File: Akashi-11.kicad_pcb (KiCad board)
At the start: 2 copper layers, 69.9 x 74.9 mm, 2 parts, among them CN10 PPPC192LFBN-RC, CN7 PPPC192LFBN-RC

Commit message: Initial layout of PCB.
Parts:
- added C1: 0.1u, Capacitor_SMD:C_0603_1608Metric_Pad1.08x0.95mm_HandSolder, F.Cu at (170.2, 39.4)
- added C2: 1u, Capacitor_SMD:C_0603_1608Metric_Pad1.08x0.95mm_HandSolder, F.Cu at (143.5, 99.1)
- added C3: 0.1u, Capacitor_SMD:C_0603_1608Metric_Pad1.08x0.95mm_HandSolder, F.Cu at (138.4, 99.1)
- added C4: 1u, Capacitor_SMD:C_0603_1608Metric_Pad1.08x0.95mm_HandSolder, F.Cu at (144.8, 102.0)
- added C5: 0.1u, Capacitor_SMD:C_0603_1608Metric_Pad1.08x0.95mm_HandSolder, F.Cu at (140.1, 69.8)
- added C6: 22u, Capacitor_THT:CP_Radial_D5.0mm_P2.50mm, F.Cu at (166.4, 47.0)
- added C7: 0.1u, Capacitor_SMD:C_0603_1608Metric_Pad1.08x0.95mm_HandSolder, F.Cu at (153.7, 39.4)
- added C8: 0.1u, Capacitor_SMD:C_0603_1608Metric_Pad1.08x0.95mm_HandSolder, F.Cu at (147.3, 69.8)
- added C9: 10u, Capacitor_THT:CP_Radial_D5.0mm_P2.50mm, F.Cu at (153.7, 47.0)
- added D1: D_Schottky, Capacitor_SMD:C_0603_1608Metric_Pad1.08x0.95mm_HandSolder, F.Cu at (142.2, 102.0)
- added D2: D_Schottky, Capacitor_SMD:C_0603_1608Metric_Pad1.08x0.95mm_HandSolder, F.Cu at (143.5, 105.4)
- added D3: LED, LED_THT:LED_D4.0mm, F.Cu at (130.8, 43.2)
- added J1: Conn_02x20_Odd_Even, Connector_PinHeader_2.54mm:PinHeader_2x20_P2.54mm_Vertical, F.Cu at (171.5, 106.7)
- added L1: LQH5BPN4R7N38L, LOCAL_LIB:LQH5BPN100M38L, F.Cu at (175.8, 40.6)
- added L2: LQH5BPN100M38L, LOCAL_LIB:LQH5BPN100M38L, F.Cu at (147.3, 40.6)
- added R1: 1k, Capacitor_SMD:C_0603_1608Metric_Pad1.08x0.95mm_HandSolder, F.Cu at (130.8, 48.3)
- added R2: 61.9, Capacitor_SMD:C_0603_1608Metric_Pad1.08x0.95mm_HandSolder, F.Cu at (151.1, 50.8)
- added R3: 2.15, Capacitor_SMD:C_0603_1608Metric_Pad1.08x0.95mm_HandSolder, F.Cu at (146.1, 50.8)
- added R4: 39, Capacitor_SMD:C_0603_1608Metric_Pad1.08x0.95mm_HandSolder, F.Cu at (176.5, 105.4)
- added R5: 330, Capacitor_SMD:C_0603_1608Metric_Pad1.08x0.95mm_HandSolder, F.Cu at (147.3, 102.0)
- added SW1: SW, Button_Switch_THT:SW_TH_Tactile_Omron_B3F-10xx, F.Cu at (118.7, 40.9)
- added U1: MAX6934AQH+D, Package_LCC:PLCC-44_THT-Socket, F.Cu at (146.1, 77.5)
- added U2: MAX4719EUB+, LOCAL_LIB:MAX4719EUB, F.Cu at (157.5, 104.1)
- added U3: TPS613221ADBV, Package_TO_SOT_SMD:SOT-23-5, F.Cu at (175.3, 48.3)
- added U4: TLV61046ADB, Package_TO_SOT_SMD:SOT-23-6, F.Cu at (147.2, 46.7)
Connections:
- CN10 pad 11: unconnected-(CN10-Pad11) -> /D0
- CN10 pad 12: unconnected-(CN10-Pad12) -> /SPI1_MOSI
- CN10 pad 13: unconnected-(CN10-Pad13) -> /D1
- CN10 pad 15: unconnected-(CN10-Pad15) -> /TIM1_CH1N
- CN10 pad 16: unconnected-(CN10-Pad16) -> /D2
- CN10 pad 17: unconnected-(CN10-Pad17) -> /D3
- CN10 pad 19: unconnected-(CN10-Pad19) -> /D4
- CN10 pad 20: unconnected-(CN10-Pad20) -> GND
- CN10 pad 21: unconnected-(CN10-Pad21) -> /TIM2_CH1
- CN10 pad 22: unconnected-(CN10-Pad22) -> /D5
- CN10 pad 23: unconnected-(CN10-Pad23) -> /TIM1_CH1
- CN10 pad 24: unconnected-(CN10-Pad24) -> /D6
- CN10 pad 25: unconnected-(CN10-Pad25) -> /D7
- CN10 pad 27: unconnected-(CN10-Pad27) -> /D8
- CN10 pad 29: unconnected-(CN10-Pad29) -> /KEY3
- CN10 pad 31: unconnected-(CN10-Pad31) -> /KEY2
- CN10 pad 32: unconnected-(CN10-Pad32) -> GND
- CN10 pad 33: unconnected-(CN10-Pad33) -> /KEY1
- CN10 pad 36: unconnected-(CN10-Pad36) -> /SPI1_SCK
- CN10 pad 9: unconnected-(CN10-Pad9) -> GND
- CN7 pad 1: unconnected-(CN7-Pad1) -> /LOAD
- CN7 pad 12: unconnected-(CN7-Pad12) -> +3V3
- CN7 pad 14: unconnected-(CN7-Pad14) -> Net-(CN7-Pad14)
- CN7 pad 16: unconnected-(CN7-Pad16) -> +3V3
- CN7 pad 19: unconnected-(CN7-Pad19) -> GND
- CN7 pad 2: unconnected-(CN7-Pad2) -> Net-(CN7-Pad2)
- CN7 pad 20: unconnected-(CN7-Pad20) -> GND
- CN7 pad 22: unconnected-(CN7-Pad22) -> GND
- CN7 pad 3: unconnected-(CN7-Pad3) -> /BLANK
- CN7 pad 8: unconnected-(CN7-Pad8) -> GND
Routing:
- net unconnected-(CN7-Pad1): track 2.69 -> 0.00 mm
- net /LOAD: track 0.00 -> 2.69 mm
- net unconnected-(CN7-Pad3): track 2.69 -> 0.00 mm
- net /BLANK: track 0.00 -> 2.69 mm
- added copper zone on B.Cu, net GND
- added copper zone on F.Cu, net GND
- removed copper zone on B.Cu, net unconnected-(CN10-Pad9)
- removed copper zone on F.Cu, net unconnected-(CN10-Pad9)

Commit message: Routing finished
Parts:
- added JP1: Jumper_2_Bridged, Jumper:SolderJumper-2_P1.3mm_Bridged_RoundedPad1.0x1.5mm, F.Cu at (175.9, 51.4)
- added JP2: Jumper_2_Bridged, Jumper:SolderJumper-2_P1.3mm_Bridged_RoundedPad1.0x1.5mm, F.Cu at (151.8, 61.0)
- added TP1: TestPoint, TestPoint:TestPoint_Loop_D1.80mm_Drill1.0mm_Beaded, F.Cu at (142.2, 106.7)
- added TP10: TestPoint, TestPoint:TestPoint_Loop_D1.80mm_Drill1.0mm_Beaded, F.Cu at (158.8, 99.1)
- added TP11: TestPoint, TestPoint:TestPoint_Loop_D1.80mm_Drill1.0mm_Beaded, F.Cu at (163.8, 105.4)
- added TP12: TestPoint, TestPoint:TestPoint_Loop_D1.80mm_Drill1.0mm_Beaded, F.Cu at (157.5, 106.7)
- added TP13: TestPoint, TestPoint:TestPoint_Loop_D1.80mm_Drill1.0mm_Beaded, F.Cu at (146.1, 100.3)
- added TP2: TestPoint, TestPoint:TestPoint_Loop_D1.80mm_Drill1.0mm_Beaded, F.Cu at (130.8, 105.4)
- added TP3: TestPoint, TestPoint:TestPoint_Loop_D1.80mm_Drill1.0mm_Beaded, F.Cu at (181.6, 48.3)
- added TP4: TestPoint, TestPoint:TestPoint_Loop_D1.80mm_Drill1.0mm_Beaded, F.Cu at (181.6, 43.2)
- added TP5: TestPoint, TestPoint:TestPoint_Loop_D1.80mm_Drill1.0mm_Beaded, F.Cu at (176.5, 104.1)
- added TP6: TestPoint, TestPoint:TestPoint_Loop_D1.80mm_Drill1.0mm_Beaded, F.Cu at (176.5, 72.4)
- added TP7: TestPoint, TestPoint:TestPoint_Loop_D1.80mm_Drill1.0mm_Beaded, F.Cu at (151.8, 55.9)
- added TP8: TestPoint, TestPoint:TestPoint_Loop_D1.80mm_Drill1.0mm_Beaded, F.Cu at (127.0, 69.8)
- added TP9: TestPoint, TestPoint:TestPoint_Loop_D1.80mm_Drill1.0mm_Beaded, F.Cu at (127.0, 63.5)
- moved C6 16.5 mm to (181.6, 53.4), turned to -90 degrees
- moved R4 16.3 mm to (160.4, 102.6), turned to 180 degrees
- moved D1 6.35 mm to (135.9, 102.0)
- moved C2 6.35 mm to (137.2, 99.1)
- moved C3 6.35 mm to (132.1, 99.1)
- moved C4 6.35 mm to (138.4, 102.0)
- moved D2 6.35 mm to (137.2, 105.4)
- moved R5 6.35 mm to (141.0, 102.0)
- moved U2 5.24 mm to (152.4, 102.9)
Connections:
- C6 pad 1: +3V3 -> Net-(C6-Pad1)
- C9 pad 1: +24V -> Net-(C9-Pad1)
- CN10 pad 11: /D0 -> /KD0
- CN10 pad 13: /D1 -> /KD1
- CN10 pad 16: /D2 -> /KD2
- CN10 pad 17: /D3 -> /KD3
- CN10 pad 19: /D4 -> /KD4
- CN10 pad 22: /D5 -> /KD5
- CN10 pad 24: /D6 -> /KD6
- CN10 pad 25: /D7 -> /KD7
- CN10 pad 27: /D8 -> /KD8
- J1 pad 12: /D8 -> /KD8
- J1 pad 14: /D7 -> /KD7
- J1 pad 16: /D6 -> /KD6
- J1 pad 18: /D5 -> /KD5
- J1 pad 20: /D4 -> /KD4
- J1 pad 22: /D3 -> /KD3
- J1 pad 24: /D2 -> /KD2
- J1 pad 26: /D1 -> /KD1
- J1 pad 28: /D0 -> /KD0
- R2 pad 1: +24V -> Net-(C9-Pad1)
- U3 pad 4: +3V3 -> Net-(C6-Pad1)
- U4 pad 5: +24V -> Net-(C9-Pad1)
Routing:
- net /TIM2_CH1: track 0.00 -> 62.1 mm
- net +BATT: track 0.00 -> 56.4 mm
- net /SPI1_SCK: track 0.00 -> 52.2 mm
- net /TIM1_CH1: track 0.00 -> 47.8 mm
- net /LOAD: track 2.69 -> 46.9 mm
- net /Seg_a: track 0.00 -> 41.4 mm
- net /TIM1_CH1N: track 0.00 -> 40.6 mm
- net /SPI1_MOSI: track 0.00 -> 39.2 mm
- net Net-(CN7-Pad14): track 0.00 -> 38.8 mm
- net /BLANK: track 2.69 -> 40.9 mm
- net /D8: track 0.00 -> 32.1 mm
- net /D0: track 0.00 -> 27.8 mm
- net /D7: track 0.00 -> 26.4 mm
- net /Seg_g: track 0.00 -> 25.5 mm
- net +24V: track 0.00 -> 25.4 mm
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- added copper zone on B.Cu, net +3V3
- removed copper zone on B.Cu, net GND
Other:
- board text added: "+24V"
- board text added: "+3.3V"
- board text added: "-2.5V"
- board text added: "Akashi-11 v1.0.0 https://github.com/suikan4github/Akashi-11 (C) Seiichi Horie 2022"
- board text added: "BLANK"
- board text added: "GND"
- board text added: "H1"
- board text added: "H2"
- board text added: "LOAD"
- board text added: "RESET"
- board text added: "SPI1_MOSI"
- board text added: "SPI1_SCK"
- board text added: "TIM1_CH1"
- board text added: "TIM1_CH1N"
- board text added: "TIM2_CH1"

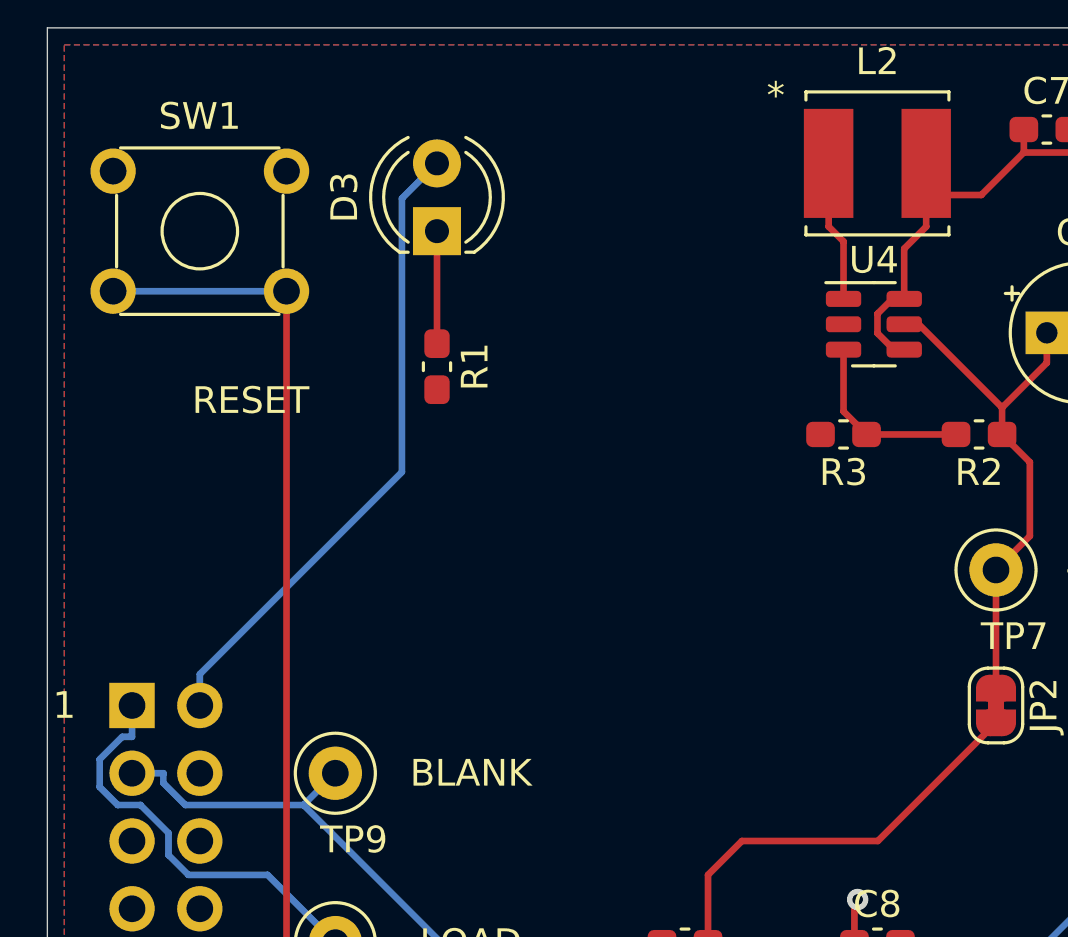
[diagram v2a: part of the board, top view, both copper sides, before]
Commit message: Add EN24 signal and description of README
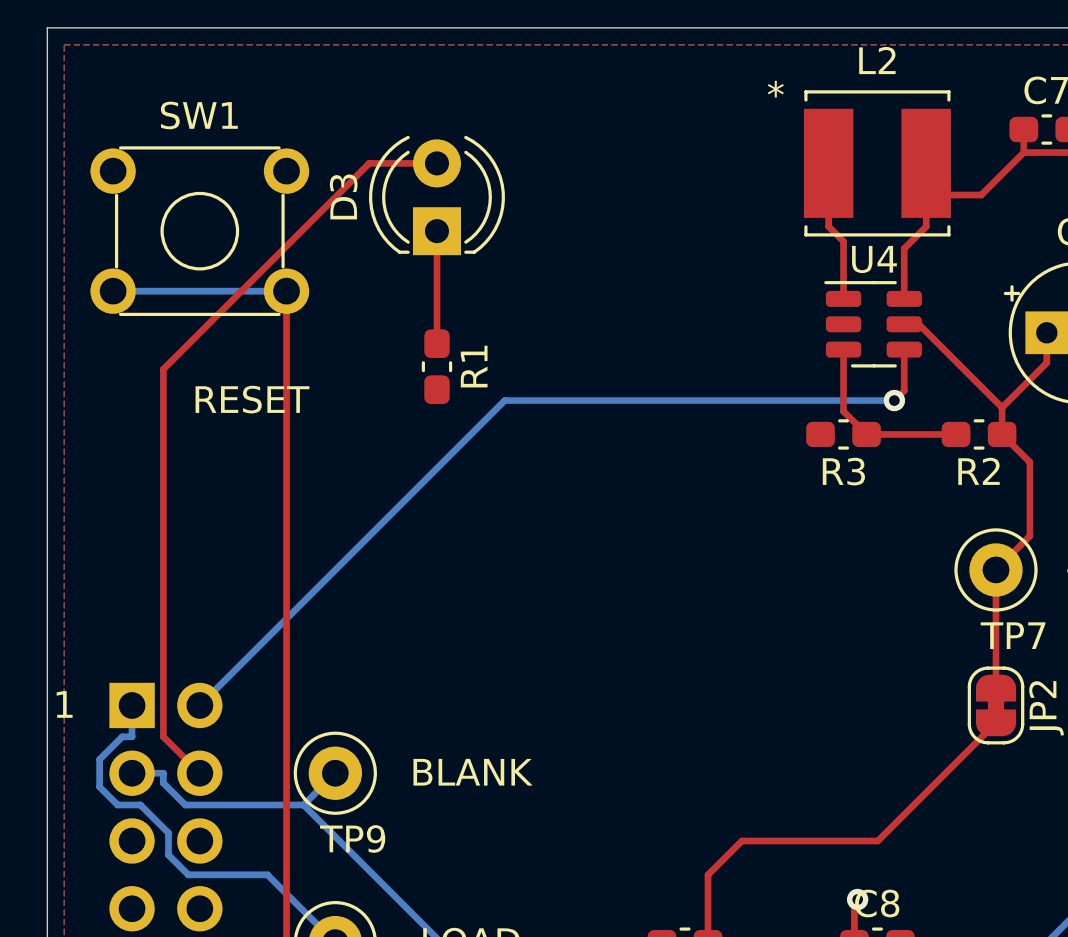
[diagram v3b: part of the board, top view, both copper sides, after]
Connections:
- CN7 pad 2: Net-(CN7-Pad2) -> /EN24
- CN7 pad 4: unconnected-(CN7-Pad4) -> /STATUS
- D3 pad 2: Net-(CN7-Pad2) -> /STATUS
- U4 pad 4: +BATT -> /EN24
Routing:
- net /EN24: track 0.00 -> 32.8 mm, vias 0 -> 1
- net /STATUS: track 0.00 -> 29.2 mm
- net Net-(CN7-Pad2): track 24.0 -> 0.00 mm
- net +BATT: track 56.4 -> 53.2 mm
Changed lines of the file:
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@@
   (net 2 "GND")
   (net 3 "-2V5")
-  (net 4 "unconnected-(CN7-Pad4)")
+  (net 4 "/EN24")
   (net 5 "unconnected-(CN7-Pad5)")
   (net 6 "unconnected-(CN7-Pad6)")
@@
   (net 18 "unconnected-(CN7-Pad18)")
   (net 19 "/LOAD")
-  (net 20 "Net-(CN7-Pad2)")
+  (net 20 "/STATUS")
   (net 21 "unconnected-(CN7-Pad21)")
   (net 22 "/BLANK")
@@
       (net 95 "Net-(R2-Pad2)") (pinfunction "FB") (pintype "input"))
     (pad "4" smd roundrect (at 1.1375 0.95) (size 1.325 0.6) (layers "F.Cu" "F.Paste" "F.Mask") (roundrect_rratio 0.25)
-      (net 1 "+BATT") (pinfunction "EN") (pintype "input"))
+      (net 4 "/EN24") (pinfunction "EN") (pintype "input"))
     (pad "5" smd roundrect (at 1.1375 0) (size 1.325 0.6) (layers "F.Cu" "F.Paste" "F.Mask") (roundrect_rratio 0.25)
       (net 128 "Net-(C9-Pad1)") (pinfunction "VOUT") (pintype "power_out"))
@@
       (net 71 "Net-(D3-Pad1)") (pinfunction "K") (pintype "passive"))
     (pad "2" thru_hole circle (at 2.54 0 90) (size 1.8 1.8) (drill 0.9) (layers *.Cu *.Mask)
-      (net 20 "Net-(CN7-Pad2)") (pinfunction "A") (pintype "passive"))
+      (net 20 "/STATUS") (pinfunction "A") (pintype "passive"))
     (model "${KICAD6_3DMODEL_DIR}/LED_THT.3dshapes/LED_D4.0mm.wrl"
       (offset (xyz 0 0 0))
@@
       (net 19 "/LOAD") (pinfunction "Pin_1") (pintype "passive"))
     (pad "2" thru_hole oval locked (at -2.54 0 180) (size 1.7 1.7) (drill 1) (layers *.Cu *.Mask)
-      (net 20 "Net-(CN7-Pad2)") (pinfunction "Pin_2") (pintype "passive"))
+      (net 4 "/EN24") (pinfunction "Pin_2") (pintype "passive"))
     (pad "3" thru_hole oval locked (at 0 -2.54 180) (size 1.7 1.7) (drill 1) (layers *.Cu *.Mask)
       (net 22 "/BLANK") (pinfunction "Pin_3") (pintype "passive"))
     (pad "4" thru_hole oval locked (at -2.54 -2.54 180) (size 1.7 1.7) (drill 1) (layers *.Cu *.Mask)
-      (net 4 "unconnected-(CN7-Pad4)") (pinfunction "Pin_4") (pintype "passive+no_connect"))
+      (net 20 "/STATUS") (pinfunction "Pin_4") (pintype "passive"))
     (pad "5" thru_hole oval locked (at 0 -5.08 180) (size 1.7 1.7) (drill 1) (layers *.Cu *.Mask)
       (net 5 "unconnected-(CN7-Pad5)") (pinfunction "Pin_5") (pintype "passive+no_connect"))
@@
   (segment (start 169.2823 59.7799) (end 170.0901 58.9721) (width 0.25) (layer "F.Cu") (net 1))
   (segment (start 149.1488 41.8249) (end 151.2151 41.8249) (width 0.25) (layer "F.Cu") (net 1))
-  (segment (start 147.321 46.2799) (end 147.321 47.0045) (width 0.25) (layer "F.Cu") (net 1))
   (segment (start 148.325 43.8336) (end 148.325 45.72) (width 0.25) (layer "F.Cu") (net 1))
-  (segment (start 148.325 45.72) (end 147.8809 45.72) (width 0.25) (layer "F.Cu") (net 1))
-  (segment (start 147.321 47.0045) (end 147.9365 47.62) (width 0.25) (layer "F.Cu") (net 1))
   (segment (start 152.8075 40.2325) (end 170.18 40.2325) (width 0.25) (layer "F.Cu") (net 1))
-  (segment (start 147.8809 45.72) (end 147.321 46.2799) (width 0.25) (layer "F.Cu") (net 1))
   (segment (start 168.915 59.7799) (end 169.2823 59.7799) (width 0.25) (layer "F.Cu") (net 1))
   (segment (start 170.0901 58.9721) (end 170.0901 41.1374) (width 0.25) (layer "F.Cu") (net 1))
   (segment (start 151.2151 41.8249) (end 152.8075 40.2325) (width 0.25) (layer "F.Cu") (net 1))
-  (segment (start 147.9365 47.62) (end 148.325 47.62) (width 0.25) (layer "F.Cu") (net 1))
   (segment (start 170.5875 40.64) (end 170.18 40.2325) (width 0.25) (layer "F.Cu") (net 1))
   (segment (start 136.2975 99.06) (end 136.2975 100.5337) (width 0.25) (layer "F.Cu") (net 3))
@@
   (segment (start 132.9425 100.9412) (end 132.9425 103.2775) (width 0.25) (layer "F.Cu") (net 3))
   (segment (start 138.43 92.71) (end 136.2975 94.8425) (width 0.25) (layer "F.Cu") (net 3))
+  (segment (start 148.325 49.16) (end 147.955 49.53) (width 0.25) (layer "F.Cu") (net 4))
+  (segment (start 148.325 47.62) (end 148.325 49.16) (width 0.25) (layer "F.Cu") (net 4))
+  (via (at 147.955 49.53) (size 0.8) (drill 0.4) (layers "F.Cu" "B.Cu") (net 4))
+  (segment (start 133.35 49.53) (end 121.92 60.96) (width 0.25) (layer "B.Cu") (net 4))
+  (segment (start 147.955 49.53) (end 133.35 49.53) (width 0.25) (layer "B.Cu") (net 4))
   (segment (start 138.43 101.145) (end 140.97 101.145) (width 0.25) (layer "F.Cu") (net 8))
   (segment (start 138.0225 104.0041) (end 137.6592 103.6408) (width 0.25) (layer "F.Cu") (net 12))
@@
   (segment (start 118.8412 64.6904) (end 119.6945 64.6904) (width 0.25) (layer "B.Cu") (net 19))
   (segment (start 119.6945 64.6904) (end 120.7448 65.7407) (width 0.25) (layer "B.Cu") (net 19))
-  (segment (start 121.92 59.7849) (end 129.4952 52.2097) (width 0.25) (layer "B.Cu") (net 20))
-  (segment (start 121.92 60.96) (end 121.92 59.7849) (width 0.25) (layer "B.Cu") (net 20))
-  (segment (start 129.4952 41.9548) (end 130.81 40.64) (width 0.25) (layer "B.Cu") (net 20))
-  (segment (start 129.4952 52.2097) (end 129.4952 41.9548) (width 0.25) (layer "B.Cu") (net 20))
+  (segment (start 120.554511 48.355489) (end 128.27 40.64) (width 0.25) (layer "F.Cu") (net 20))
+  (segment (start 121.92 63.5) (end 120.554511 62.134511) (width 0.25) (layer "F.Cu") (net 20))
+  (segment (start 128.27 40.64) (end 130.81 40.64) (width 0.25) (layer "F.Cu") (net 20))
+  (segment (start 120.554511 62.134511) (end 120.554511 48.355489) (width 0.25) (layer "F.Cu") (net 20))
   (segment (start 137.3936 76.2748) (end 137.3936 80.494) (width 0.25) (layer "B.Cu") (net 22))
   (segment (start 120.5551 63.5) (end 120.5551 63.8672) (width 0.25) (layer "B.Cu") (net 22))

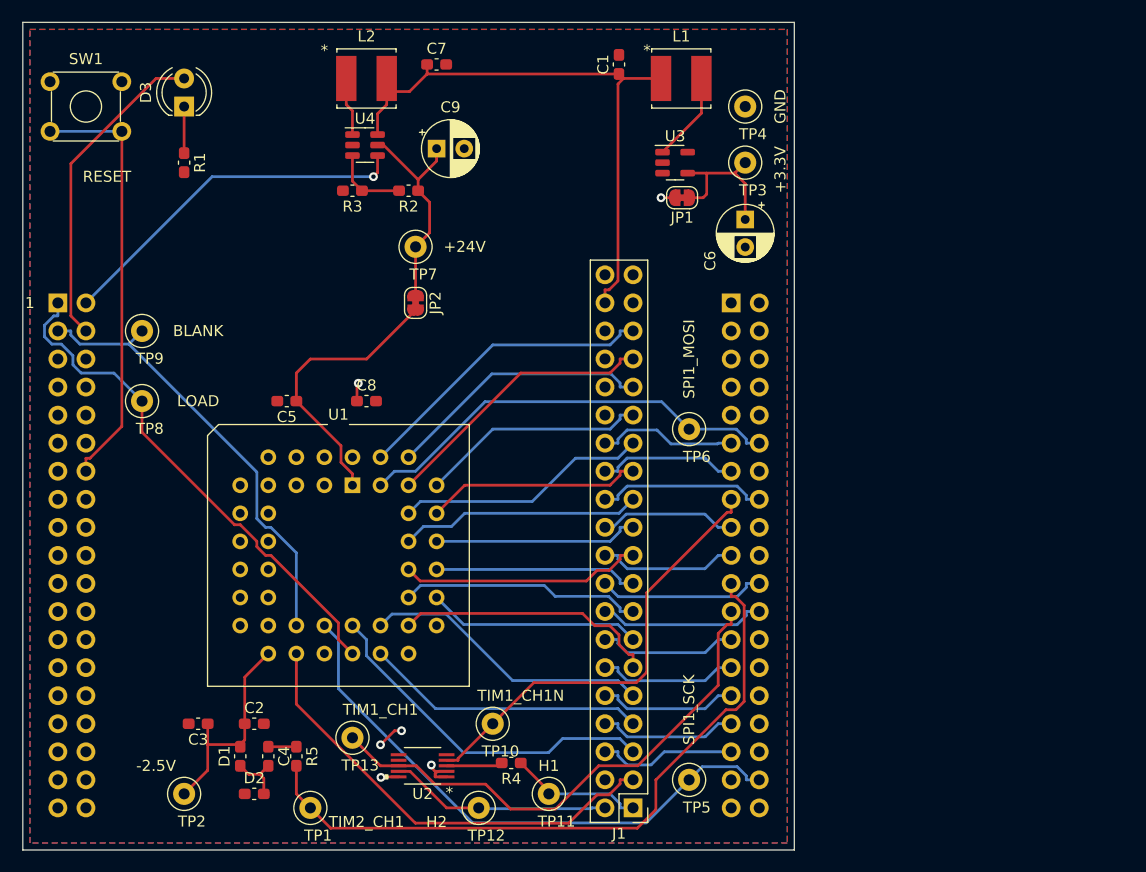
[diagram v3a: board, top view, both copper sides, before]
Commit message: Layout refined.
Footprint of L is updated for hand soldering.
Electric Capacitor foot print is now same with EL-210-MOD.
Heater resiters are now same withe EL-210-MOD.
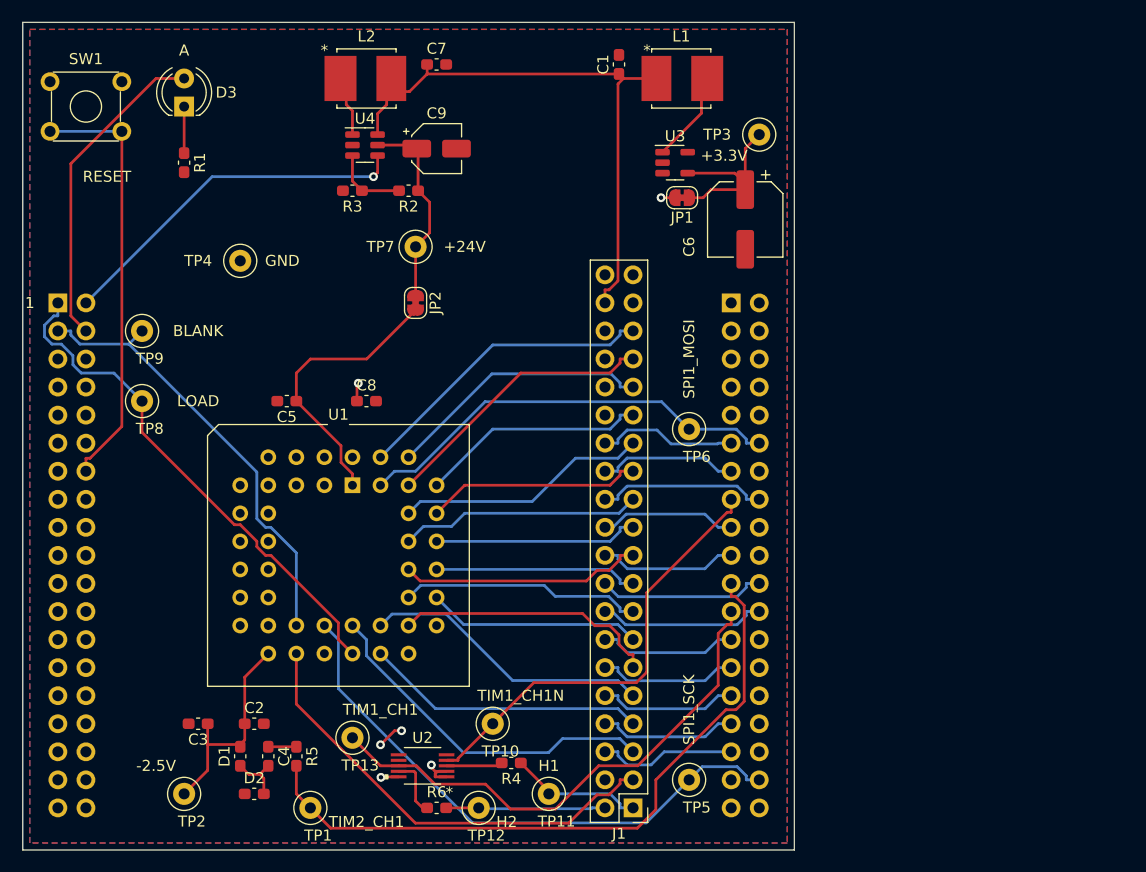
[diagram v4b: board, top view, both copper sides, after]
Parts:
- added R6: 18, Capacitor_SMD:C_0603_1608Metric_Pad1.08x0.95mm_HandSolder, F.Cu at (153.7, 106.7)
- C6: value 22u -> UZG0J220MCL1GB; footprint Capacitor_THT:CP_Radial_D5.0mm_P2.50mm -> Capacitor_SMD:CP_Elec_6.3x3
- C9: value 10u -> UZG1H100MCL1GB; footprint Capacitor_THT:CP_Radial_D5.0mm_P2.50mm -> Capacitor_SMD:CP_Elec_4x3.9
- R4: value 39 -> 18
- moved TP4 47.8 mm to (135.9, 57.1)
- moved TP3 2.84 mm to (182.9, 45.7)
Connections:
- U2 pad 9: /H2 -> Net-(U2-Pad9)
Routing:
- net /H2: track 20.1 -> 14.4 mm
- net Net-(U2-Pad9): track 0.00 -> 5.67 mm
- net Net-(C6-Pad1): track 13.8 -> 16.5 mm
- net Net-(C9-Pad1): track 19.9 -> 18.0 mm
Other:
- board text added: "A"
